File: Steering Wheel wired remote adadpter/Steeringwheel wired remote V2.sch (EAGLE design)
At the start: 8 parts

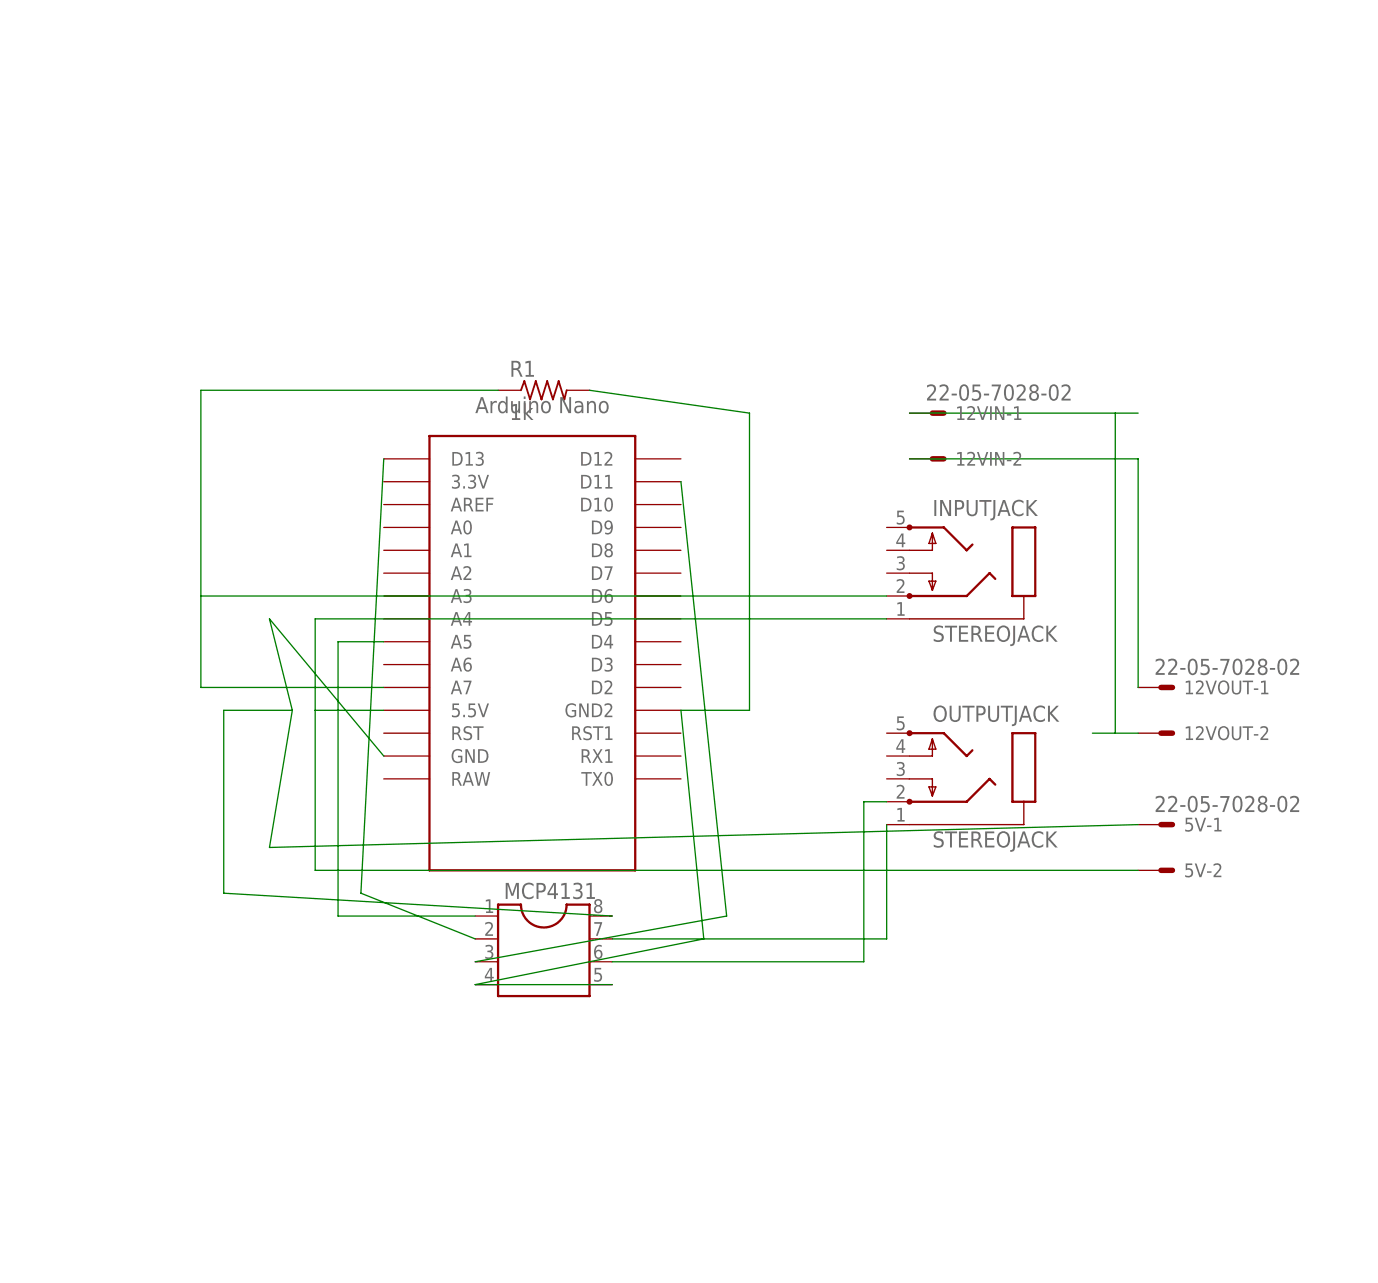
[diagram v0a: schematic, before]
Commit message: 3 pin jacks added
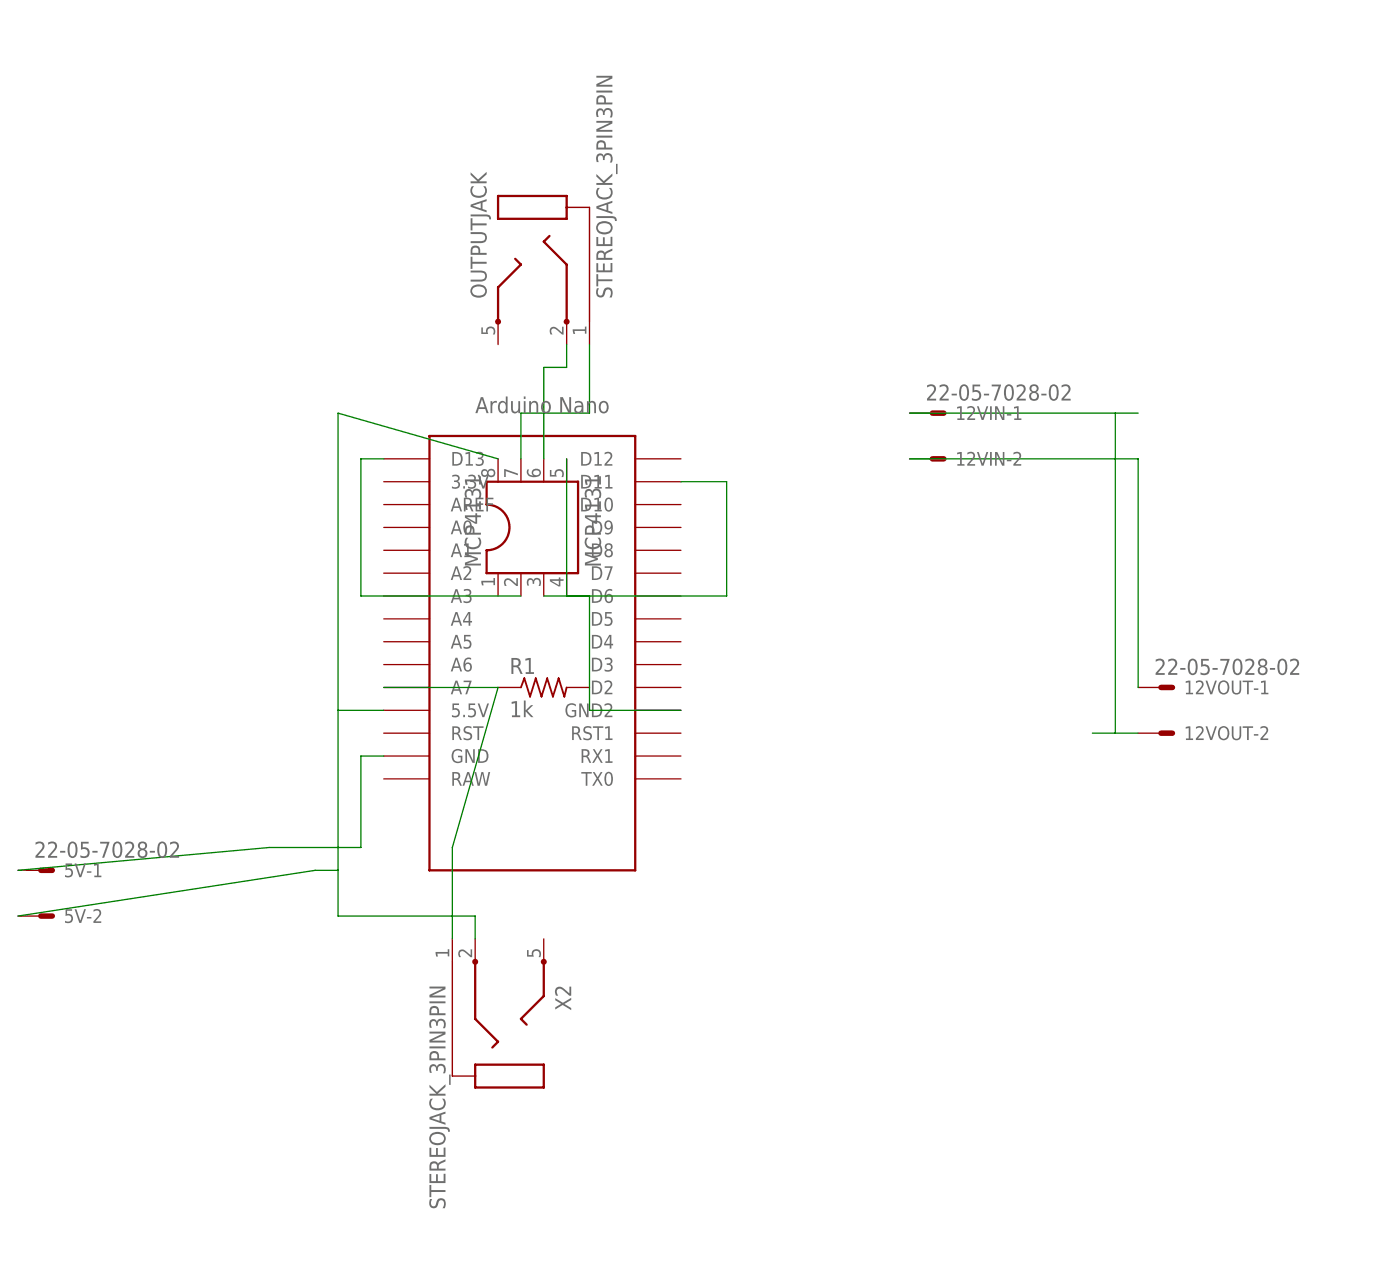
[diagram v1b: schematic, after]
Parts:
- removed INPUTJACK: STEREOJACK, adafruit:STEREOJACK
- removed U$1: NANO, Arduino-clone:NANO
- added U$2: NANO, my_lib:NANO
- added X2: STEREOJACK_3PIN3PIN, my_lib:STEREOJACK_3PIN3PIN
- IC1: value (none) -> MCP4131
- OUTPUTJACK: value STEREOJACK -> STEREOJACK_3PIN3PIN; device adafruit:STEREOJACK -> my_lib:STEREOJACK_3PIN3PIN
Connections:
- removed net N$10: 5V-2.S, INPUTJACK.1, U$1.5.5V
- removed net N$11: IC1.!CS, U$1.A5
- new net N$2: IC1.SCK, U$2.D13
- net N$1: now also IC1.SDI, U$2.D11; no longer IC1.GND, IC1.P0A, R1.2, U$1.GND2
- net N$3: now also IC1.GND, IC1.P0A, R1.2, U$2.GND2; no longer IC1.SCK, U$1.D13
- net N$4: now also R1.1, U$2.A7, X2.1; no longer IC1.SDI, U$1.D11
- net N$6: now also 5V-2.S, IC1.VCC, U$2.5.5V, X2.2; no longer INPUTJACK.2, R1.1, U$1.A7
- net N$7: now also U$2.GND; no longer IC1.VCC, U$1.GND
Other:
- moved on the sheet: 5V-1, 5V-2, R1

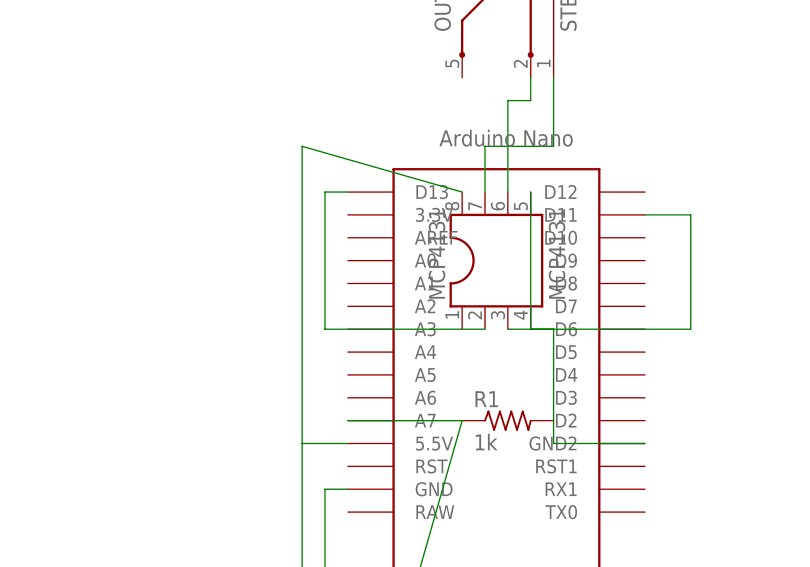
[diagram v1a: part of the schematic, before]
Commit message: GND copper poor and .024 traces
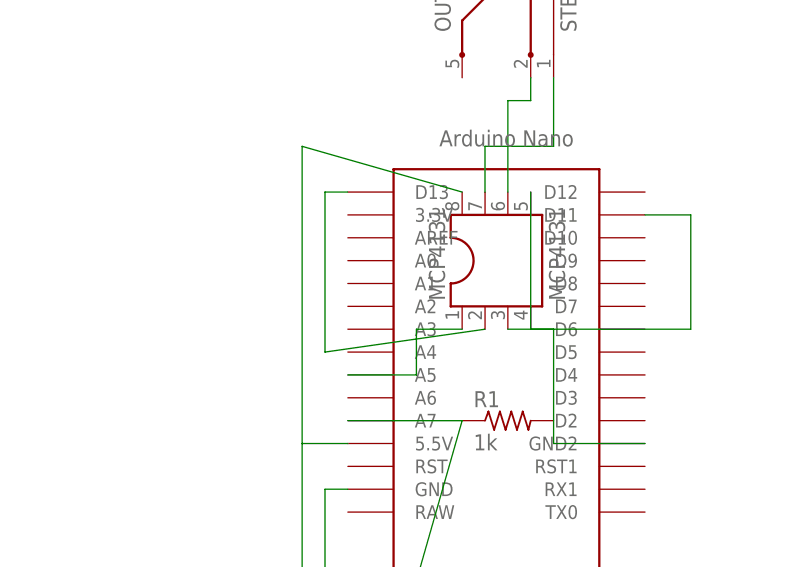
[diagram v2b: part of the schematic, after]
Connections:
- removed net N$3: IC1.GND, IC1.P0A, R1.2, U$2.GND2
- removed net N$7: 5V-1.S, U$2.GND
- new net GND: 5V-1.S, IC1.GND, IC1.P0A, R1.2, U$2.GND, U$2.GND2
- new net N$10: IC1.!CS, U$2.A5
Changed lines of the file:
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@@
 <?xml version="1.0" encoding="utf-8"?>
 <!DOCTYPE eagle SYSTEM "eagle.dtd">
-<eagle version="7.5.0">
+<eagle version="7.2.0">
 <drawing>
 <settings>
@@
 </busses>
 <nets>
-<net name="N$7" class="0">
-<segment>
-<pinref part="5V" gate="-1" pin="S"/>
-<wire x1="-58.42" y1="38.1" x2="-30.48" y2="40.64" width="0.1524" layer="91"/>
-<wire x1="-30.48" y1="40.64" x2="-20.32" y2="40.64" width="0.1524" layer="91"/>
-<wire x1="-20.32" y1="40.64" x2="-20.32" y2="50.8" width="0.1524" layer="91"/>
-<pinref part="U$2" gate="G$1" pin="GND"/>
-<wire x1="-20.32" y1="50.8" x2="-17.78" y2="50.8" width="0.1524" layer="91"/>
-</segment>
-</net>
 <net name="N$8" class="0">
 <segment>
@@
 </segment>
 </net>
-<net name="N$3" class="0">
+<net name="GND" class="0">
 <segment>
 <pinref part="IC1" gate="G$1" pin="P0A"/>
@@
 <wire x1="5.08" y1="68.58" x2="5.08" y2="58.42" width="0.1524" layer="91"/>
 </segment>
+<segment>
+<pinref part="5V" gate="-1" pin="S"/>
+<wire x1="-58.42" y1="38.1" x2="-30.48" y2="40.64" width="0.1524" layer="91"/>
+<wire x1="-30.48" y1="40.64" x2="-20.32" y2="40.64" width="0.1524" layer="91"/>
+<wire x1="-20.32" y1="40.64" x2="-20.32" y2="50.8" width="0.1524" layer="91"/>
+<pinref part="U$2" gate="G$1" pin="GND"/>
+<wire x1="-20.32" y1="50.8" x2="-17.78" y2="50.8" width="0.1524" layer="91"/>
+</segment>
 </net>
 <net name="N$1" class="0">
@@
 <segment>
 <pinref part="IC1" gate="G$1" pin="SCK"/>
-<wire x1="-2.54" y1="68.58" x2="-20.32" y2="68.58" width="0.1524" layer="91"/>
-<wire x1="-20.32" y1="68.58" x2="-20.32" y2="83.82" width="0.1524" layer="91"/>
+<wire x1="-2.54" y1="68.58" x2="-20.32" y2="66.04" width="0.1524" layer="91"/>
+<wire x1="-20.32" y1="66.04" x2="-20.32" y2="83.82" width="0.1524" layer="91"/>
 <pinref part="U$2" gate="G$1" pin="D13"/>
 <wire x1="-20.32" y1="83.82" x2="-17.78" y2="83.82" width="0.1524" layer="91"/>
@@
 </segment>
 </net>
+<net name="N$10" class="0">
+<segment>
+<pinref part="IC1" gate="G$1" pin="!CS"/>
+<wire x1="-5.08" y1="68.58" x2="-10.16" y2="68.58" width="0.1524" layer="91"/>
+<wire x1="-10.16" y1="68.58" x2="-10.16" y2="63.5" width="0.1524" layer="91"/>
+<pinref part="U$2" gate="G$1" pin="A5"/>
+<wire x1="-10.16" y1="63.5" x2="-17.78" y2="63.5" width="0.1524" layer="91"/>
+</segment>
+</net>
